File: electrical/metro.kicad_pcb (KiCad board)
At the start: 4 copper layers, 28 x 30 mm, 37 parts, among them J1 Conn_01x02, J2 Conn_01x02, J3 Conn_01x02, J4 Conn_01x03, Q1 AO3401A, U1 MCP73831T-2ACI/OT, U2 ATTINY1616-MN, U3 DRV2605LDGS, U4 XC6206P332MR-G

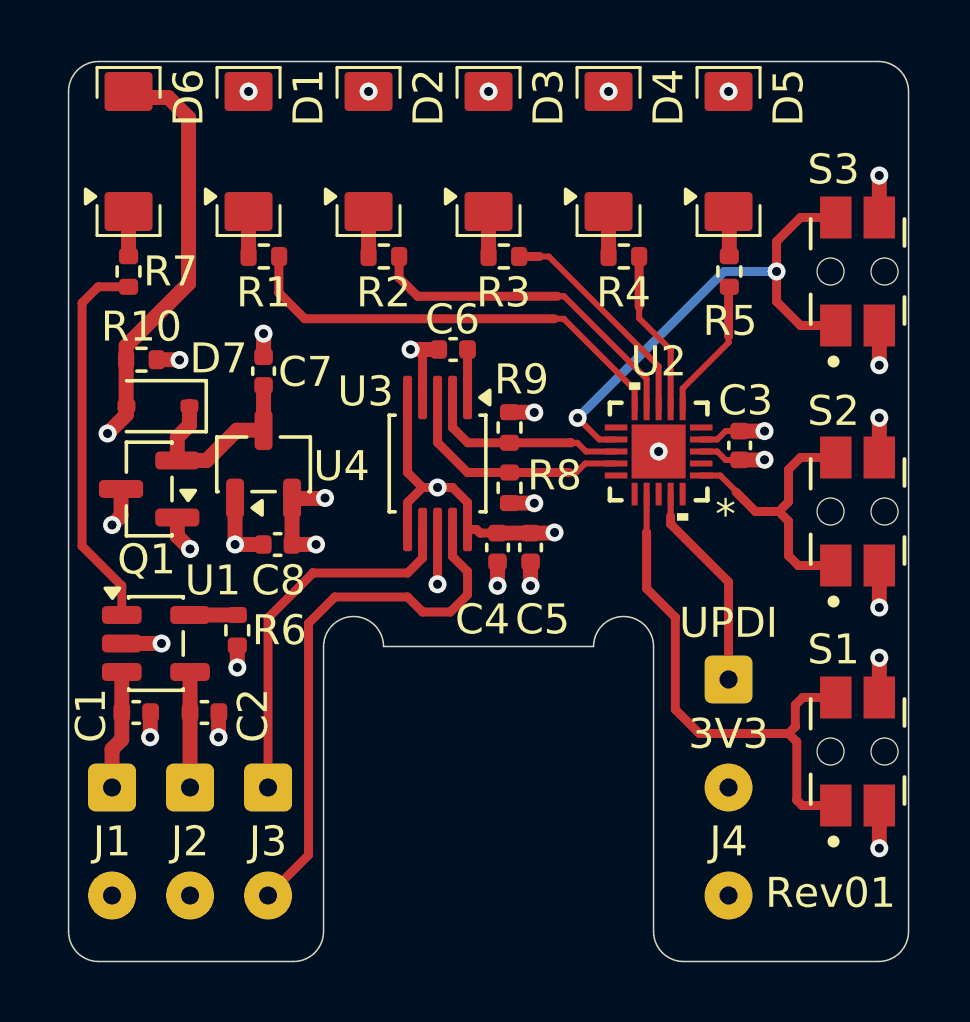
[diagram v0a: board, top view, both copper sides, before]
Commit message: rev 2 board. larger components
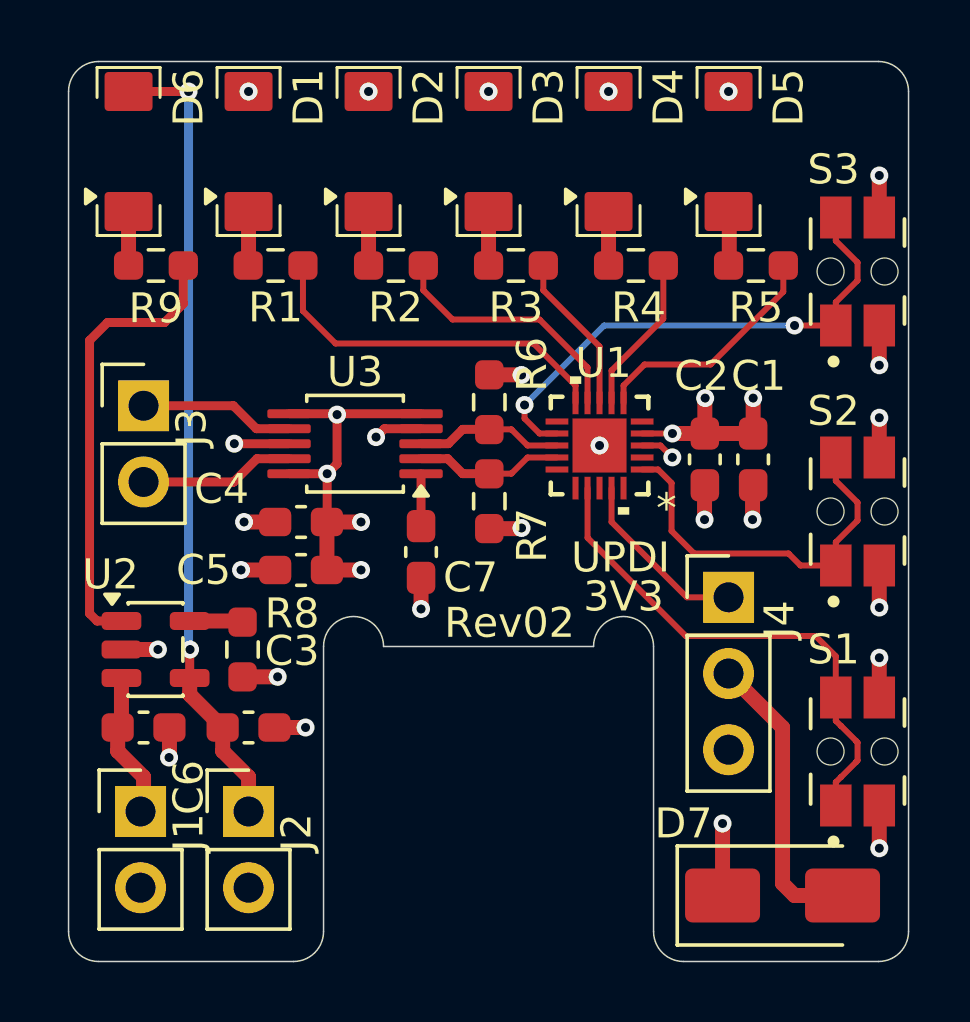
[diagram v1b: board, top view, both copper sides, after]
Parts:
- removed the C7 at (46.5, 80.3)
- removed C8: 1μF, Capacitor_SMD:C_0402_1005Metric
- removed Q1: AO3401A, Package_TO_SOT_SMD:SOT-23
- removed R10: 100kR, Resistor_SMD:R_0402_1005Metric
- removed U4: XC6206P332MR-G, Package_TO_SOT_SMD:SOT-23-3
- added C1: 1μF, Capacitor_SMD:C_0603_1608Metric_Pad1.08x0.95mm_HandSolder, F.Cu at (62.8, 83.3)
- C2: renamed from C3; footprint Capacitor_SMD:C_0402_1005Metric -> Capacitor_SMD:C_0603_1608Metric_Pad1.08x0.95mm_HandSolder
- C3: renamed from C2; footprint Capacitor_SMD:C_0402_1005Metric -> Capacitor_SMD:C_0603_1608Metric_Pad1.08x0.95mm_HandSolder
- C4, C5: footprint Capacitor_SMD:C_0402_1005Metric -> Capacitor_SMD:C_0603_1608Metric_Pad1.08x0.95mm_HandSolder
- C6: renamed from C1; footprint Capacitor_SMD:C_0402_1005Metric -> Capacitor_SMD:C_0603_1608Metric_Pad1.08x0.95mm_HandSolder
- C7: renamed from C6; footprint Capacitor_SMD:C_0402_1005Metric -> Capacitor_SMD:C_0603_1608Metric_Pad1.08x0.95mm_HandSolder
- D7: value 1N5819WS -> D_Schottky; footprint Diode_SMD:D_SOD-323 -> Diode_SMD:D_SMA
- J1, J2, J3: footprint Connector_Wire:SolderWire-0.1sqmm_1x02_P3.6mm_D0.4mm_OD1mm -> Connector_PinHeader_2.54mm:PinHeader_1x02_P2.54mm_Vertical
- J4: footprint Connector_Wire:SolderWire-0.1sqmm_1x03_P3.6mm_D0.4mm_OD1mm -> Connector_PinHeader_2.54mm:PinHeader_1x03_P2.54mm_Vertical
- R1, R2, R3, R4, R5: footprint Resistor_SMD:R_0402_1005Metric -> Resistor_SMD:R_0603_1608Metric_Pad0.98x0.95mm_HandSolder
- R6: renamed from R8; footprint Resistor_SMD:R_0402_1005Metric -> Resistor_SMD:R_0603_1608Metric_Pad0.98x0.95mm_HandSolder
- R7: renamed from R9; footprint Resistor_SMD:R_0402_1005Metric -> Resistor_SMD:R_0603_1608Metric_Pad0.98x0.95mm_HandSolder
- R8: renamed from R6; footprint Resistor_SMD:R_0402_1005Metric -> Resistor_SMD:R_0603_1608Metric_Pad0.98x0.95mm_HandSolder
- R9: renamed from R7; footprint Resistor_SMD:R_0402_1005Metric -> Resistor_SMD:R_0603_1608Metric_Pad0.98x0.95mm_HandSolder
- moved D7 26.4 mm to (63.8, 97.8), turned to 0 degrees
- moved J3 13.4 mm to (42.5, 81.5), turned to 0 degrees
- moved C5 7.69 mm to (47.8, 87.0), turned to 180 degrees
- moved C7 6.83 mm to (51.8, 86.3), turned to -90 degrees
- moved C4 6.60 mm to (47.8, 85.3), turned to 180 degrees
- moved R6 2.93 mm to (54.0, 81.4), turned to 90 degrees
- moved U3 2.83 mm to (49.5, 82.7), turned to 180 degrees
- moved J4 2.74 mm to (62.0, 87.9), turned to 0 degrees
- moved R7 2.55 mm to (54.0, 84.7), turned to -90 degrees
- moved J2 2.11 mm to (46.0, 95.0), turned to 0 degrees
- moved U1 1.98 mm to (57.7, 82.8)
- moved C3 1.55 mm to (46.0, 92.2)
- moved C2 1.25 mm to (61.2, 83.3)
- moved J1 1.24 mm to (42.4, 95.0), turned to 0 degrees
- moved R9 0.93 mm to (42.9, 76.8), turned to 180 degrees
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- renumbered U2 to U1, U1 to U2
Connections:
- C2 pad 1: +3V3 -> +BATT
- C4 pad 1: +3V3 -> +BATT
- C5 pad 1: +3V3 -> +BATT
- D1 pad 2: +3V3 -> +BATT
- D2 pad 2: +3V3 -> +BATT
- D3 pad 2: +3V3 -> +BATT
- D4 pad 2: +3V3 -> +BATT
- D5 pad 2: +3V3 -> +BATT
- D7 pad 1: /REG IN -> +BATT
- D7 pad 2: +VBUS -> Net-(D7-A)
- J4 pad 2: +3V3 -> Net-(D7-A)
- R6 pad 1: /SCL -> /SDA
- R6 pad 2: +3V3 -> +BATT
- R7 pad 1: /SDA -> /SCL
- R7 pad 2: +3V3 -> +BATT
- U1 pad 4: +3V3 -> +BATT
- U3 pad 10: +3V3 -> +BATT
- U3 pad 2: /SDA -> /SCL
- U3 pad 3: /SCL -> /SDA
- U3 pad 5: +3V3 -> +BATT
- U3 pad 6: +3V3 -> +BATT
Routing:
- net +3V3: track 17.5 -> 0.00 mm, vias 12 -> 0
- net +BATT: track 14.1 -> 28.6 mm, vias 1 -> 15
- net /MOTOR-: track 18.1 -> 5.18 mm
- net Net-(D7-A): track 0.00 -> 9.91 mm
- net /MOTOR+: track 12.6 -> 5.17 mm
- net /REG IN: track 6.76 -> 0.00 mm
- net +VBUS: track 31.9 -> 26.8 mm
- net /SW2: track 9.46 -> 12.9 mm
- net /LED5: track 4.68 -> 8.07 mm
- net /SCL: track 7.99 -> 4.94 mm
- net /LED1: track 15.0 -> 12.2 mm
- net /LED2: track 11.4 -> 8.55 mm
- net /LIPO STAT: track 12.7 -> 15.2 mm
- net /LED3: track 7.59 -> 5.36 mm
- net /SDA: track 6.78 -> 4.94 mm
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- added copper zone on In2.Cu, net +BATT
- removed copper zone on In2.Cu, net +3V3
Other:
- board text added: "Rev02"
- board text removed: "Rev01"
